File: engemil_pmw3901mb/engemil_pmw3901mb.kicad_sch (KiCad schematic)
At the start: 0 parts

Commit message: Added docs folder with datasheet, added info in title block of schematic, added info in readme
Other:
- company: (none) -> EngEmil
- title: (none) -> EngEmil PMW3901MB Module
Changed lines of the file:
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@@
 	(generator_version "9.0")
 	(paper "A4")
+	(title_block
+		(title "EngEmil PMW3901MB Module")
+		(date "2025-06-07")
+		(rev "1")
+		(company "EngEmil")
+		(comment 1 "Licensed under CERN-OHL-W-2.0")
+	)
 	(sheet_instances
 		(path "/"

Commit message: - Added BOM file - Added datasheets under docs folder - Added symbol, footprint and 3d models to lib - Added readme files to subfolder of lib - Added raw folder for lib - Designed voltage regulators and connector pin into schematic - The sensor chip is work in progress
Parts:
- added C1, C2, C3, C4: 1uF, engemil_pmw3901mb_module_footprint_library:C0805, symbol engemil_pmw3901mb_module_symbol_library:C0805C105J4RECAUTO7210
- added J1: 6130XX11121, engemil_pmw3901mb_module_footprint_library:61300811121, symbol engemil_pmw3901mb_module_symbol_library:6130XX11121_61300811121
- added U1: PMW3901MB-TXQT, QFN_01MB-TXQT_PIX, symbol engemil_pmw3901mb_module_symbol_library:PMW3901MB-TXQT
- added U2: TLV77333PDBVR, DBV0005A-IPC_A, symbol engemil_pmw3901mb_module_symbol_library:TLV77333PDBVR
- added U3: TLV77318PDBVR, DBV0005A-IPC_A, symbol engemil_pmw3901mb_module_symbol_library:TLV77318PDBVR
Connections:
- new net: U1.20 (NC), U1.21 (GND), U1.22 (NC), U1.23 (NC), U1.24 (NC), U1.25 (NC), U1.26 (NC), U1.27 (NC), U1.28 (NC), U1.29 (GND)
- new net +1V8: C4.2, U3.5 (OUT)
- new net +3.3V: C2.2, C3.2, U2.5 (OUT), U3.1 (IN), U3.3 (EN)
- new net CS: J1.5, U1.19 (NCS)
- new net GND: C1.1, C2.1, C3.1, C4.1, J1.8, U1.10 (NC), U1.11 (NC), U1.12 (NC), U1.13 (NC), U1.14 (NC), U1.5 (NC), U1.6 (NC), U1.8 (NC), U1.9 (NC), U2.2 (GND), U2.4 (NC), U3.2 (GND), U3.4 (NC)
- new net MISO: J1.3, U1.18 (MISO)
- new net MOSI: J1.4, U1.16 (MOSI)
- new net MOTION: J1.6, U1.15 (MOTION)
- new net RESET: J1.7
- new net SCLK: J1.2, U1.17 (SCLK)
- new net VCC: C1.2, J1.1, U2.1 (IN), U2.3 (EN)
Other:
- note added: "1V8 Regulator"
- note added: "3V3 Regulator"
- note added: "8-pin Connector"
- note added: "VCC/VIN range 1.4V-5.5V"

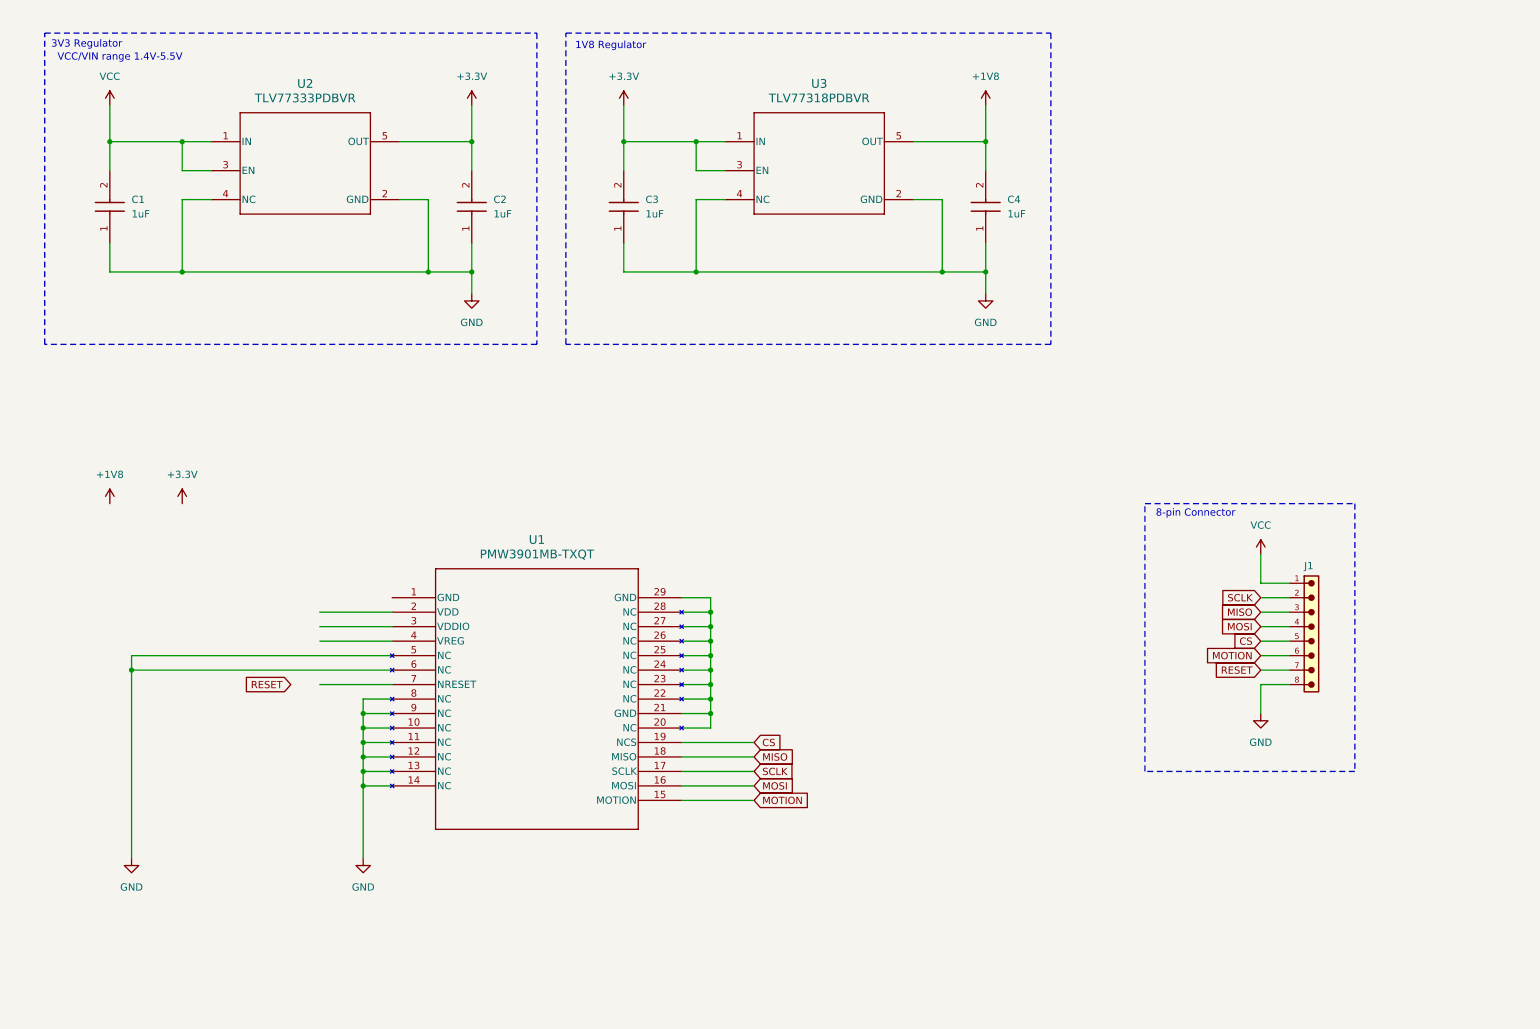
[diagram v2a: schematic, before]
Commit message: - Added more components to the BOM - Added component EDA/CAD files to the lib folder - Finished first version of Schematic
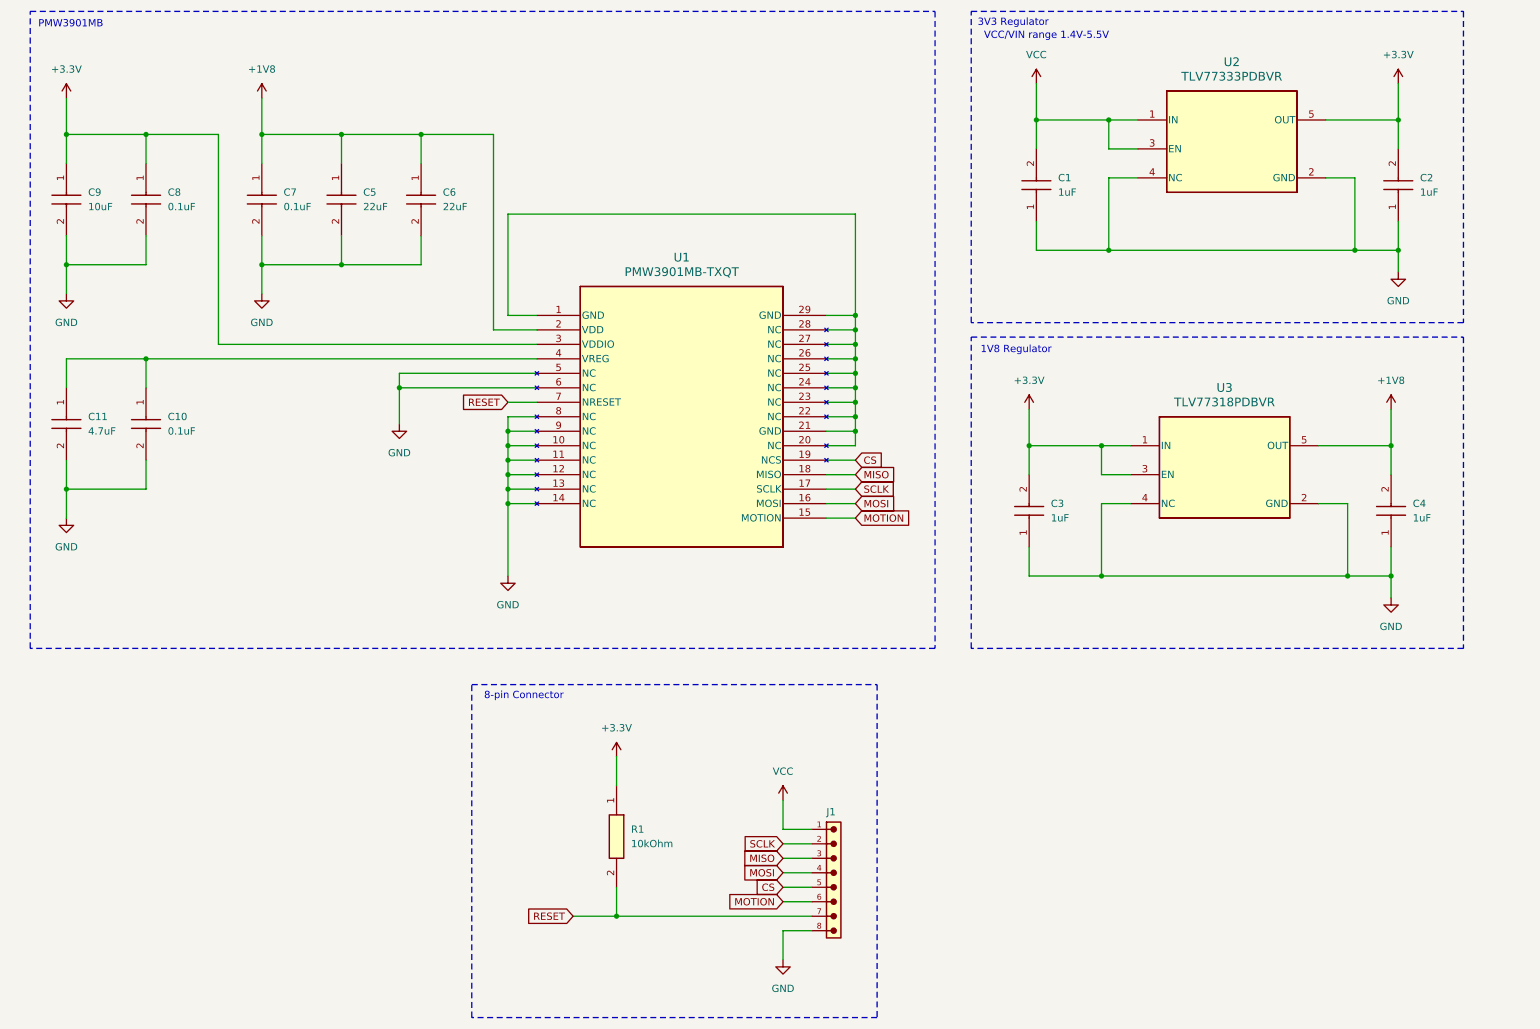
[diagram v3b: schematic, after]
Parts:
- added C10, C7, C8: 0.1uF, CAPC2012X110N, symbol engemil_pmw3901mb_module_symbol_library:C0805C104JMRECAUTO7210
- added C11: 4.7uF, C0805, symbol engemil_pmw3901mb_module_symbol_library:C0805C475K4RACAUTO7210
- added C5, C6: 22uF, C0805, symbol engemil_pmw3901mb_module_symbol_library:C0805C226M9PAC7210
- added C9: 10uF, C0805, symbol engemil_pmw3901mb_module_symbol_library:C0805C106K4PAC7210
- added R1: 10kOhm, RESC2012X60N, symbol engemil_pmw3901mb_module_symbol_library:RE0805FRE0710KL
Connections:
- net +1V8: now also U1.2 (VDD), C5.1, C6.1, C7.1
- net +3.3V: now also U1.3 (VDDIO), C8.1, C9.1, R1.1
- net GND: now also C10.2, C11.2, C5.2, C6.2, C7.2, C8.2, C9.2
- net RESET: now also U1.7 (NRESET), R1.2
- net at U1.1 (GND): now also U1.20 (NC), U1.21 (GND), U1.22 (NC), U1.23 (NC), U1.24 (NC), U1.25 (NC), U1.26 (NC), U1.27 (NC), U1.28 (NC), U1.29 (GND)
- net at U1.4 (VREG): now also C10.1, C11.1
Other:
- note added: "PMW3901MB"
- moved on the sheet: C1, C2, C3, C4, J1
